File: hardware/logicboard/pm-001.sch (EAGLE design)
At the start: 20 parts, among them K1 G5V1, T1 2SC1815

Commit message: Changed signal names.
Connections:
- net N$4 renamed MIDIINA
- net N$6 renamed 0R
- net N$8 renamed RELAYC
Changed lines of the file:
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@@
 </segment>
 </net>
-<net name="N$4" class="0">
+<net name="MIDIINA" class="0">
 <segment>
 <pinref part="R3" gate="G$1" pin="1"/>
@@
 </segment>
 </net>
-<net name="N$6" class="0">
+<net name="0R" class="0">
 <segment>
 <pinref part="T1" gate="G$1" pin="B"/>
@@
 </segment>
 </net>
-<net name="N$8" class="0">
+<net name="RELAYC" class="0">
 <segment>
 <pinref part="K1" gate="1" pin="2"/>

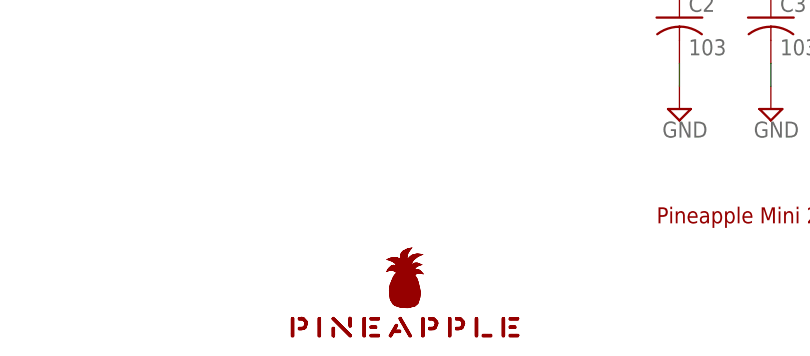
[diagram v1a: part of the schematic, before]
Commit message: Pineapple Logo (vector->bitmap), OSHW logo (silk -> copper).
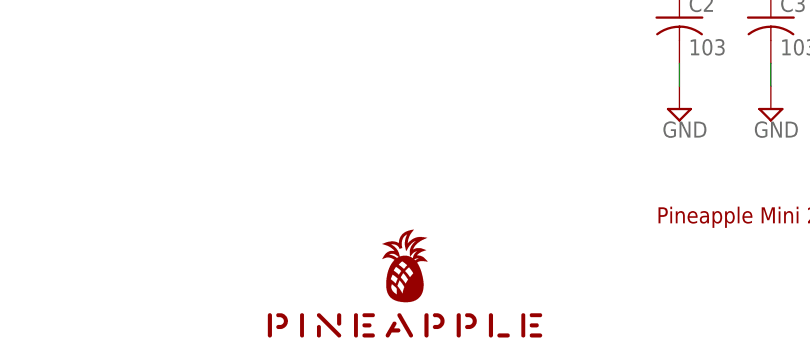
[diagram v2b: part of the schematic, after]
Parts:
- LOGO1: value OSHW-LOGOS -> OSHW-LOGOS-COPPER; device SparkFun-Aesthetics:OSHW-LOGOS -> SparkFun-Aesthetics:OSHW-LOGOS-COPPER
- U$2: value PINEAPPLELOGO2SILKMINI -> PINEAPPLE450; device pineapplelogo:PINEAPPLELOGO2SILKMINI -> pineapple:PINEAPPLE450
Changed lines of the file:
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@@
 <part name="SUPPLY8" library="supply2" deviceset="GND" device=""/>
 <part name="FRAME1" library="frames" library_urn="urn:adsk.eagle:library:229" deviceset="A4L-LOC" device=""/>
-<part name="U$2" library="pineapplelogo" deviceset="PINEAPPLELOGO2SILKMINI" device=""/>
-<part name="LOGO1" library="SparkFun-Aesthetics" deviceset="OSHW-LOGO" device="S" value="OSHW-LOGOS"/>
+<part name="U$2" library="pineapple" deviceset="PINEAPPLE450" device=""/>
+<part name="LOGO1" library="SparkFun-Aesthetics" deviceset="OSHW-LOGO" device="S-COPPER" value="OSHW-LOGOS-COPPER"/>
 </parts>
 <sheets>
